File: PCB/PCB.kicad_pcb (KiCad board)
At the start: 2 copper layers, 16.2 x 18 mm, 23 parts, among them J1 Conn_01x06_Pin, U2 A7106, U3 HT7333-3.3V, U4 STM32G031F6Px, Y1 16MHz

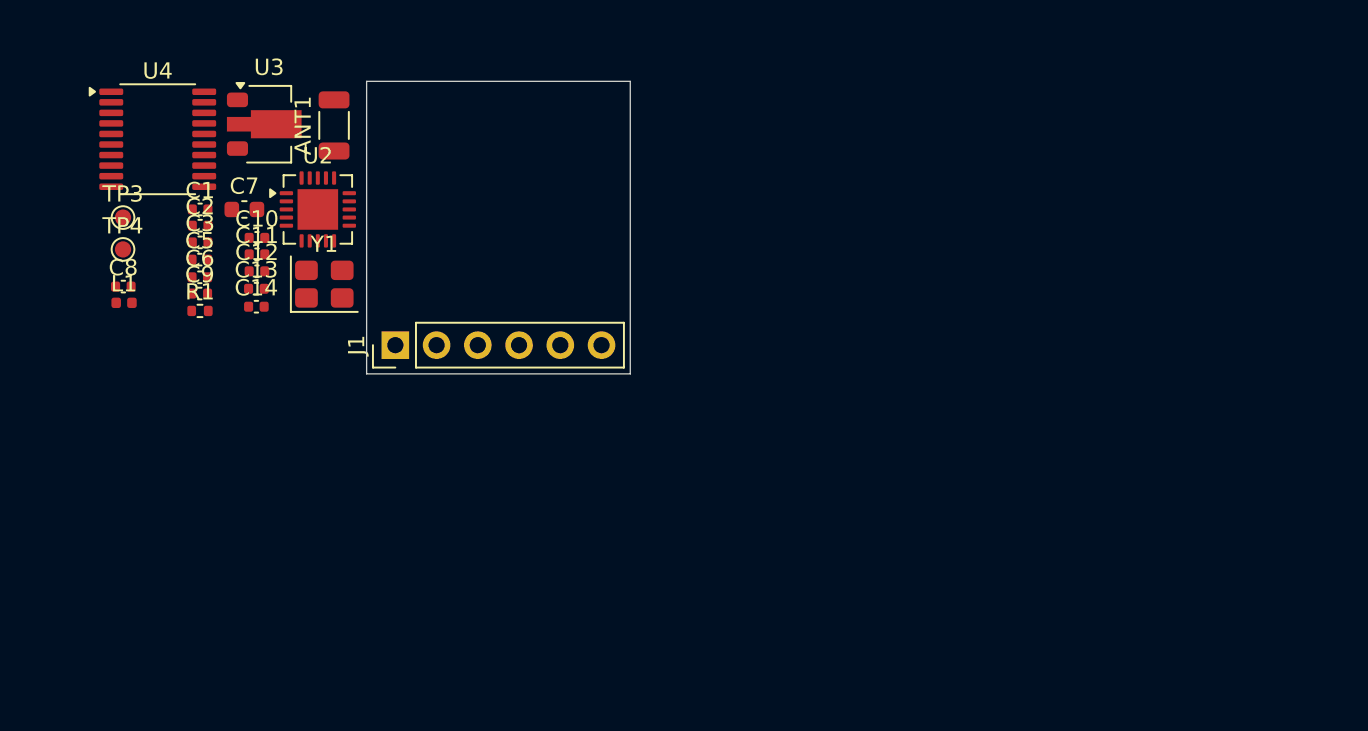
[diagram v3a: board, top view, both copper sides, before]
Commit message: Update BOM and simplifiy board
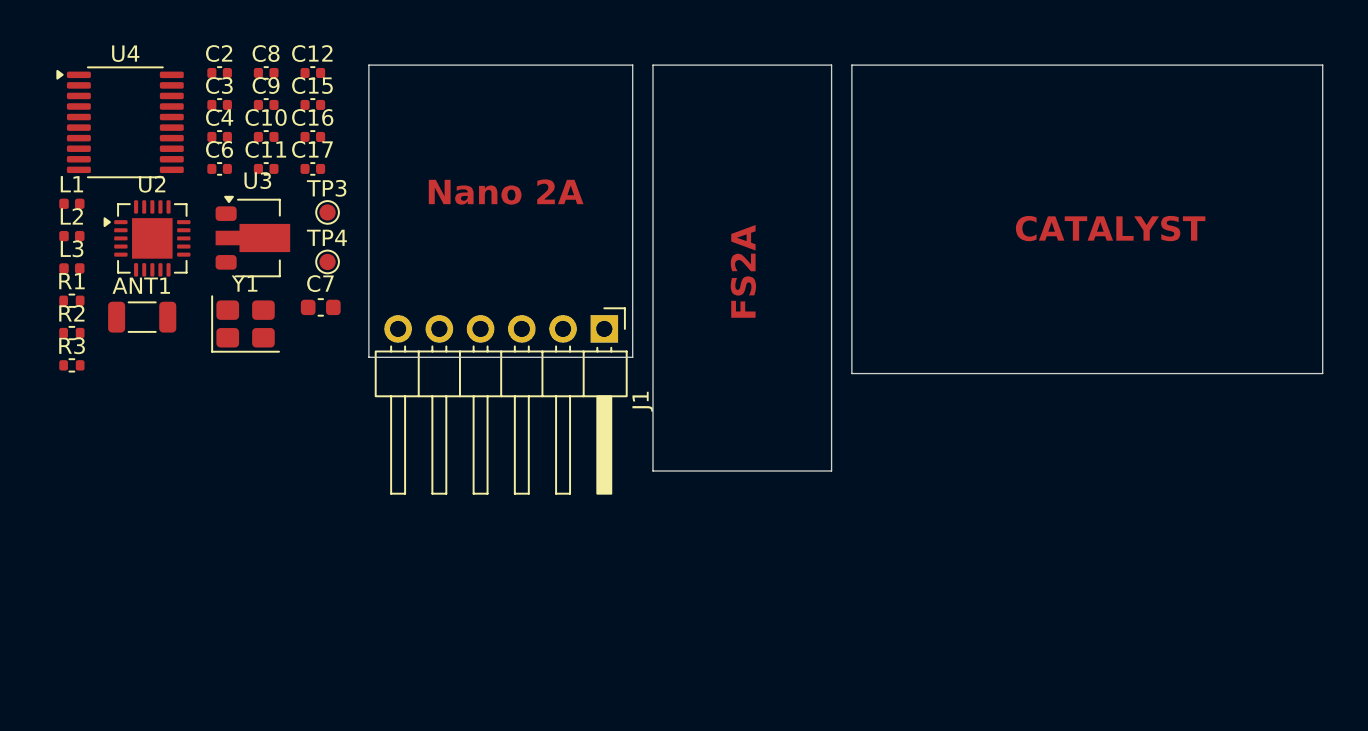
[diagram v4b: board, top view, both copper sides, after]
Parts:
- removed C1: 2.7pF, Capacitor_SMD:C_0402_1005Metric
- removed C13, C14, C5: 100nF, Capacitor_SMD:C_0402_1005Metric
- added C15: 22pF, Capacitor_SMD:C_0402_1005Metric, F.Cu at (163.5, 93.0)
- added C16: 1pF, Capacitor_SMD:C_0402_1005Metric, F.Cu at (163.5, 94.9)
- added C17: 100n, Capacitor_SMD:C_0402_1005Metric, F.Cu at (163.5, 96.9)
- added C4: 10pF, Capacitor_SMD:C_0402_1005Metric, F.Cu at (157.8, 94.9)
- added L2: 4.7nH, Inductor_SMD:L_0402_1005Metric, F.Cu at (148.7, 101.0)
- added L3: 4.7nH, Inductor_SMD:L_0402_1005Metric, F.Cu at (148.7, 103.0)
- added R2: 68k, Resistor_SMD:R_0402_1005Metric, F.Cu at (148.7, 107.0)
- added R3: 10k, Resistor_SMD:R_0402_1005Metric, F.Cu at (148.7, 109.0)
- C2, C3: value 18pF -> 8.2pF
- J1: footprint Connector_PinHeader_2.54mm:PinHeader_1x06_P2.54mm_Vertical -> Connector_PinHeader_2.54mm:PinHeader_1x06_P2.54mm_Horizontal
- L1: value 2.2nH -> 2.7nH
- moved ANT1 16.7 mm to (153.0, 106.0), turned to 0 degrees
- moved C8 15.8 mm to (160.7, 91.0)
- moved J1 12.9 mm to (181.5, 106.8), turned to -90 degrees
- moved C12 12.7 mm to (163.5, 91.0)
- moved TP4 12.6 mm to (164.5, 102.6)
- moved TP3 12.6 mm to (164.5, 99.6)
- moved C9 12.3 mm to (160.7, 93.0)
- moved U2 10.3 mm to (153.7, 101.2)
- moved C2 9.48 mm to (157.8, 91.0)
- moved C3 8.55 mm to (157.8, 93.0)
- moved R1 7.91 mm to (148.7, 105.0)
- moved C7 7.65 mm to (164.0, 105.4)
- moved U3 7.04 mm to (160.2, 101.2)
- moved L1 6.89 mm to (148.7, 99.0)
- moved C6 6.79 mm to (157.8, 96.9)
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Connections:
- ANT1 pad 2: Net-(ANT1-PCB_Trace) -> GND
- L1 pad 1: Net-(U2-RFO) -> /RF
- L1 pad 2: Net-(C1-Pad1) -> Net-(ANT1-FEED)
- U2 pad 21: (no net) -> GND
- U2 pad 3: Net-(ANT1-PCB_Trace) -> Net-(U2-RFI)
- U4 pad 16: unconnected-(U4-PA9/PA11-Pad16) -> /VBAT
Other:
- board size 16.2 x 18 mm -> 58.8 x 25 mm
- board text added: "CATALYST"
- board text added: "FS2A"
- board text added: "Nano 2A"

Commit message: Update schematic
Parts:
- added D1: SMAJ26A, Diode_SMD:D_SMA, F.Cu at (169.2, 106.2)
- added D2: LED, LED_SMD:LED_0603_1608Metric, F.Cu at (157.7, 108.8)
- added R4: 220Ω, Resistor_SMD:R_0402_1005Metric, F.Cu at (163.7, 110.7)
- J1: value Conn_01x06_Pin -> Conn_01x05_Pin; footprint Connector_PinHeader_2.54mm:PinHeader_1x06_P2.54mm_Horizontal -> Connector_PinHeader_2.54mm:PinHeader_1x05_P2.54mm_Horizontal
- moved Y1 15.9 mm to (174.0, 100.0)
- moved L1 15.0 mm to (163.7, 98.8)
- moved L2 15.0 mm to (163.7, 100.8)
- moved L3 15.0 mm to (163.7, 102.8)
- moved R1 15.0 mm to (163.7, 104.7)
- moved R2 15.0 mm to (163.7, 106.7)
- moved R3 15.0 mm to (163.7, 108.7)
- moved TP3 11.9 mm to (174.8, 105.4)
- moved TP4 11.9 mm to (174.8, 108.5)
- moved C12 8.40 mm to (171.9, 90.7)
- moved C15 8.40 mm to (171.9, 92.7)
- moved C16 8.40 mm to (171.9, 94.7)
- moved C17 8.40 mm to (171.9, 96.6)
- moved C2 8.40 mm to (166.2, 90.7)
- moved C3 8.40 mm to (166.2, 92.7)
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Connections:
- J1 pad 3: /CH4 -> /CH1
- J1 pad 4: /CH3 -> /CH2
- J1 pad 5: /CH2 -> /CH3
- U4 pad 2: unconnected-(U4-PB9/PC14-Pad2) -> Net-(U4-PB9/PC14)
- U4 pad 7: /CH4 -> unconnected-(U4-PA0-Pad7)
- Y1 pad 2: Net-(U2-XO) -> GND
- Y1 pad 3: (no net) -> Net-(U2-XO)
- Y1 pad 4: (no net) -> GND
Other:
- board size 58.8 x 25 mm -> 13.8 x 16 mm
- board text removed: "CATALYST"
- board text removed: "FS2A"
- board text removed: "Nano 2A"

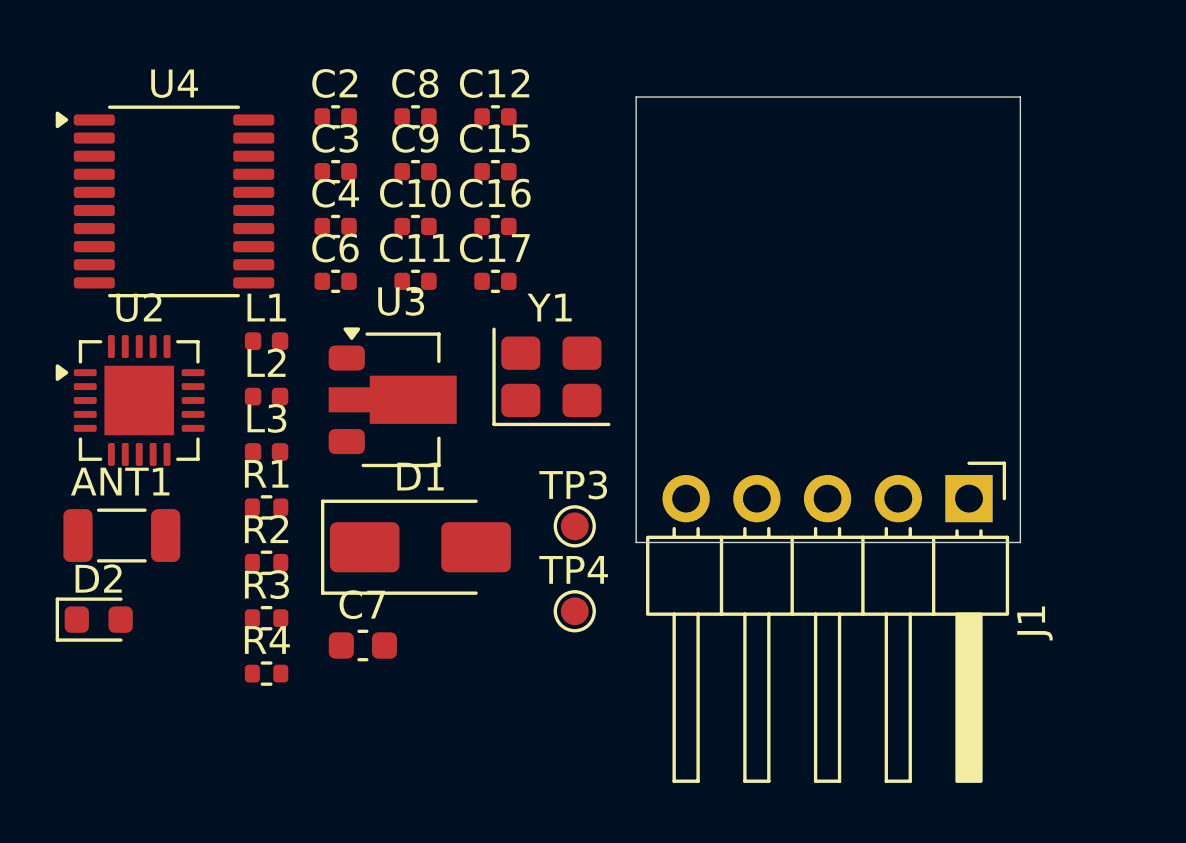
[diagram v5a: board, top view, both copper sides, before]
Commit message: Add LED and new LDO
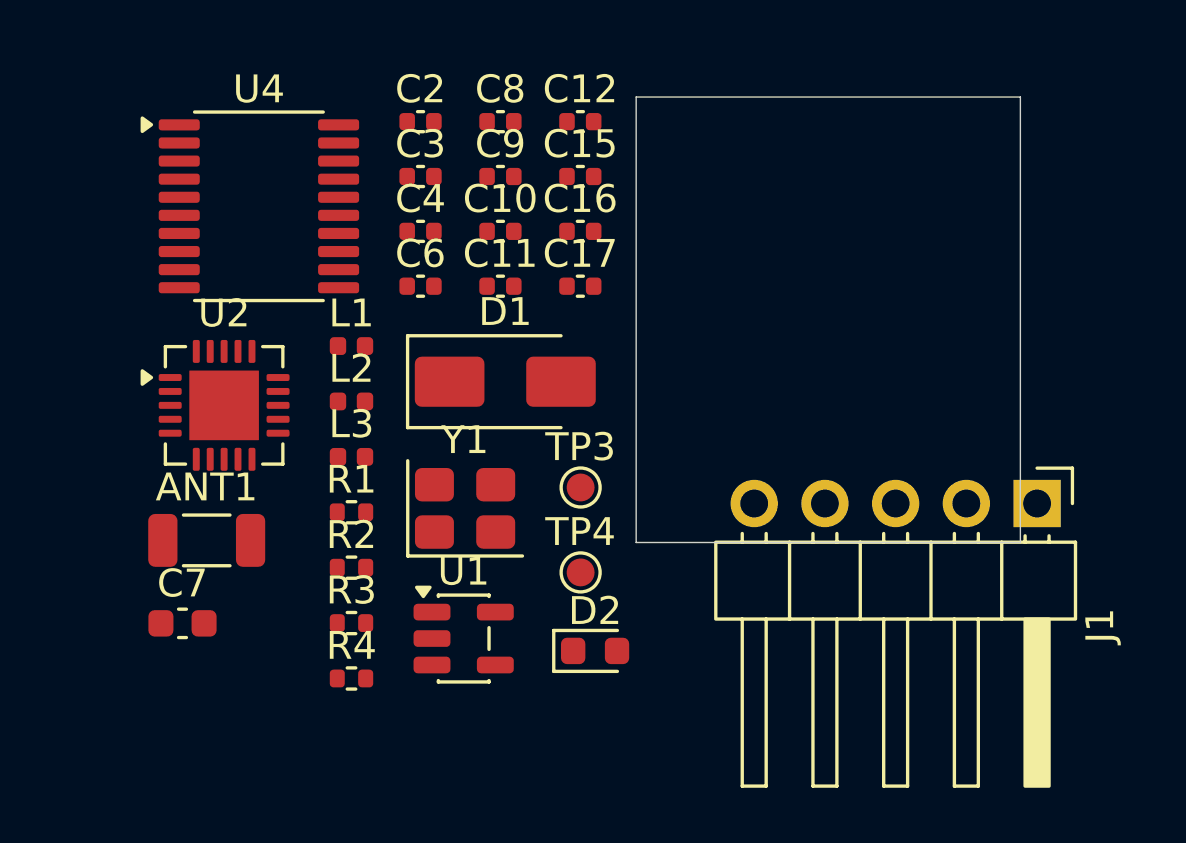
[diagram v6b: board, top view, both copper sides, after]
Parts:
- removed U3: HT7333-3.3V, Package_TO_SOT_SMD:SOT-89-3
- added U1: TPS7B6933, Package_TO_SOT_SMD:SOT-23-5, F.Cu at (170.8, 109.5)
- J1: value Conn_01x05_Pin -> Conn_01x06_Pin
- R4: value 220Ω -> 200Ω
- moved D2 17.9 mm to (175.5, 109.9)
- moved D1 6.68 mm to (172.3, 100.2)
- moved C7 6.53 mm to (160.7, 108.9)
- moved Y1 5.65 mm to (170.9, 104.8)
- moved C12 3.06 mm to (175.0, 90.9)
- moved C8 3.06 mm to (172.1, 90.9)
- moved R1 3.06 mm to (166.8, 104.9)
- moved R4 3.06 mm to (166.8, 110.9)
- moved C10 3.06 mm to (172.1, 94.8)
- moved C11 3.06 mm to (172.1, 96.8)
- moved C15 3.06 mm to (175.0, 92.9)
- moved C16 3.06 mm to (175.0, 94.8)
- moved C17 3.06 mm to (175.0, 96.8)
- moved C9 3.06 mm to (172.1, 92.9)
- moved L1 3.06 mm to (166.8, 98.9)
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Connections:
- R4 pad 1: Net-(U4-PB9/PC14) -> Net-(D2-A)
- R4 pad 2: Net-(D2-A) -> Net-(U4-PB9/PC14)
- U4 pad 10: /CH1 -> /VBAT
- U4 pad 16: /VBAT -> unconnected-(U4-PA9/PA11-Pad16)
- U4 pad 7: unconnected-(U4-PA0-Pad7) -> /CH1
- U4 pad 8: /CH3 -> /CH2
- U4 pad 9: /CH2 -> /CH3
- Y1 pad 2: GND -> Net-(U2-XO)
- Y1 pad 3: Net-(U2-XO) -> (no net)
- Y1 pad 4: GND -> (no net)

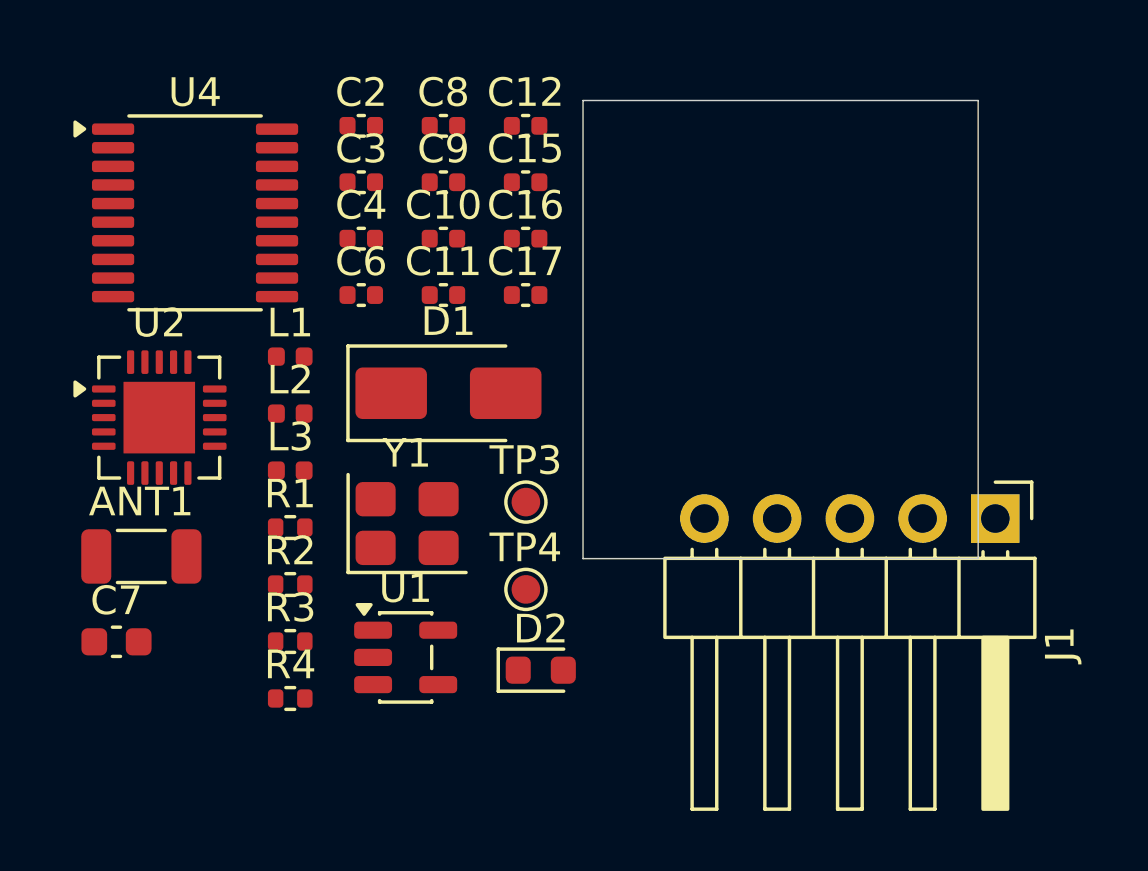
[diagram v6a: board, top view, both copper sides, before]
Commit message: Update PCB size
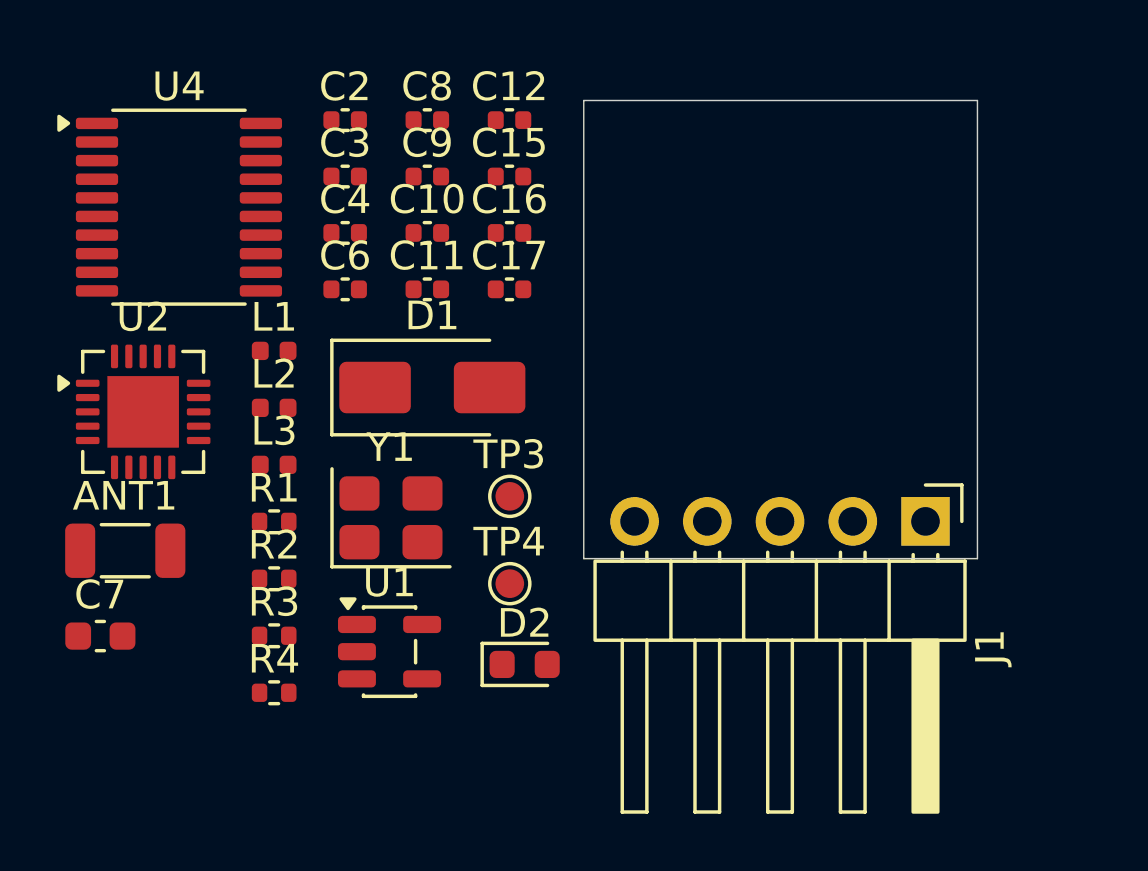
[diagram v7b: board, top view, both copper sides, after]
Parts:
- moved J1 2.44 mm to (189.0, 104.7)
- moved ANT1 0.60 mm to (161.0, 105.7)
- moved C10 0.60 mm to (171.6, 94.6)
- moved C11 0.60 mm to (171.6, 96.6)
- moved C12 0.60 mm to (174.4, 90.7)
- moved C15 0.60 mm to (174.4, 92.7)
- moved C16 0.60 mm to (174.4, 94.6)
- moved C17 0.60 mm to (174.4, 96.6)
- moved C2 0.60 mm to (168.7, 90.7)
- moved C3 0.60 mm to (168.7, 92.7)
- moved C4 0.60 mm to (168.7, 94.6)
- moved C6 0.60 mm to (168.7, 96.6)
- moved C7 0.60 mm to (160.1, 108.7)
- moved C8 0.60 mm to (171.6, 90.7)
- moved C9 0.60 mm to (171.6, 92.7)
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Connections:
- Y1 pad 3: (no net) -> GND
- Y1 pad 4: (no net) -> GND

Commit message: Update public information and crystal
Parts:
- moved J1 0.80 mm to (188.9, 103.9)
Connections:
- J1 pad 1: GND -> /CH3
- J1 pad 2: Net-(D1-A2) -> /CH2
- J1 pad 4: /CH2 -> Net-(D1-A2)
- J1 pad 5: /CH3 -> GND
- Y1 pad 3: GND -> (no net)
- Y1 pad 4: GND -> (no net)
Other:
- board size 13.8 x 16 mm -> 13.8 x 15 mm
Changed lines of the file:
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@@
 	(footprint "Connector_PinHeader_2.54mm:PinHeader_1x05_P2.54mm_Horizontal"
 		(layer "F.Cu")
-		(at 188.96 104.7 -90)
+		(at 188.95 103.9 -90)
 		(descr "Through hole angled pin header, 1x05, 2.54mm pitch, 6mm pin length, single row")
 		(tags "Through hole angled pin header THT 1x05 2.54mm single row")
@@
 			(layers "*.Cu" "*.Mask")
 			(remove_unused_layers no)
-			(net "GND")
+			(net "/CH3")
 			(pinfunction "Pin_1_1")
 			(pintype "passive")
@@
 			(layers "*.Cu" "*.Mask")
 			(remove_unused_layers no)
-			(net "Net-(D1-A2)")
+			(net "/CH2")
 			(pinfunction "Pin_2_2")
 			(pintype "passive")
@@
 			(layers "*.Cu" "*.Mask")
 			(remove_unused_layers no)
-			(net "/CH2")
+			(net "Net-(D1-A2)")
 			(pinfunction "Pin_4_4")
 			(pintype "passive")
@@
 			(layers "*.Cu" "*.Mask")
 			(remove_unused_layers no)
-			(net "/CH3")
+			(net "GND")
 			(pinfunction "Pin_5_5")
 			(pintype "passive")
@@
 			(layers "F.Cu" "F.Mask" "F.Paste")
 			(roundrect_rratio 0.208333)
-			(net "GND")
 		)
 		(pad "4" smd roundrect
@@
 			(layers "F.Cu" "F.Mask" "F.Paste")
 			(roundrect_rratio 0.208333)
-			(net "GND")
 		)
 		(embedded_fonts no)
@@
 	)
 	(gr_rect
-		(start 177.025 90)
-		(end 190.775 106)
+		(start 177.025 90.5)
+		(end 190.775 105.5)
 		(stroke
 			(width 0.05)
